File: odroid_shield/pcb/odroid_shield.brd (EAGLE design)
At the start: 83 x 48 mm, 68 parts, among them J1 AVRISP6_COMPACT, J4 ODROID_J4, U1 SINGLE-BIT_BUS_TRANSCEIVER, U10 ABM8G, U2 SINGLE-BIT_BUS_TRANSCEIVER, U3 ST1S10, U4 ATMEGA644P-20AU, U5 TS5205, U6 TCA9517MSOP8, U7 MP33926, U8 MAX21000, U9 MMA8451Q

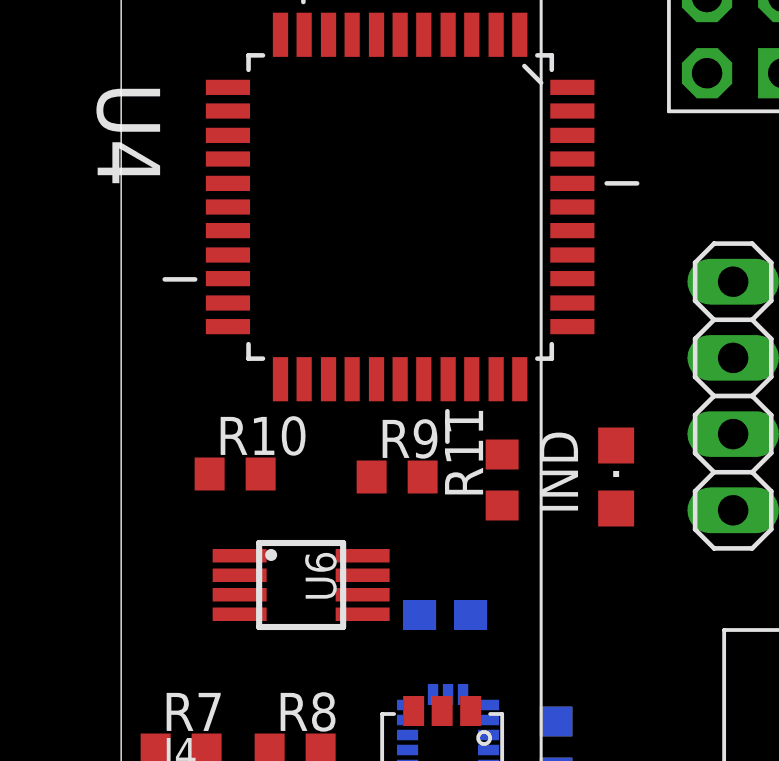
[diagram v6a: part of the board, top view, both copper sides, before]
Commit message: odroid_shield: Run schematic ERC.
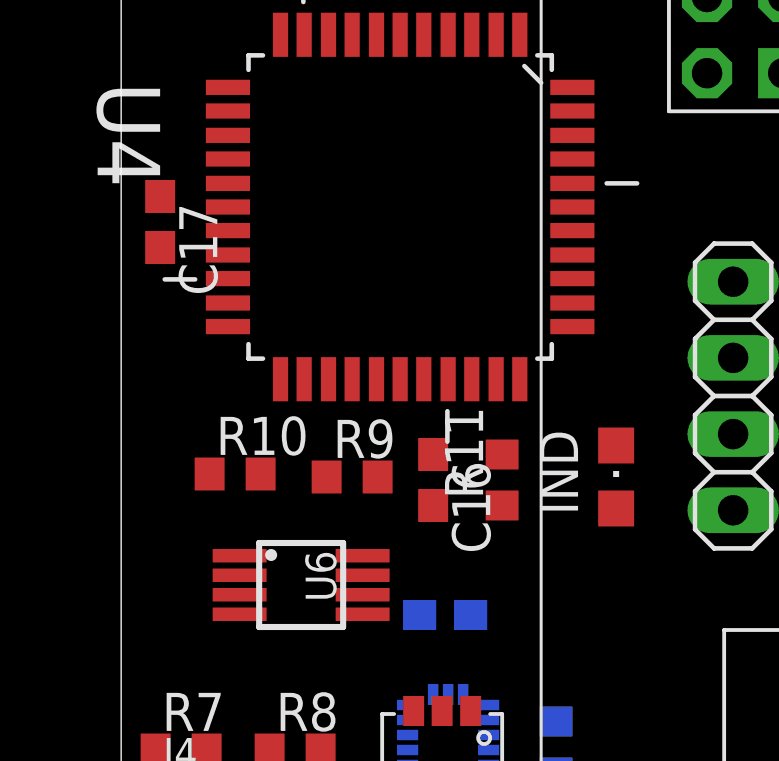
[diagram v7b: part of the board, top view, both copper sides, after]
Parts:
- added C16, C17: .1uF, rcl:C0603
- ARM: value (none) -> FLASH_RED
- D1, D2: value (none) -> 30V 2A
- IND: value (none) -> RED
- PWR: value (none) -> GREEN
- moved R9 1.50 mm to (7.70, 25.1)
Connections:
- new net N$30: C16.1, U4.29
- net +5V: now also C17.1
- net GND: now also C16.2, C17.2
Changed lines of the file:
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@@
 <element name="B+" library="odroid_shield" package="BAT_TERM" value="BAT_TERM" x="79.3" y="22.2" rot="MR0"/>
 <element name="B-" library="odroid_shield" package="BAT_TERM" value="BAT_TERM" x="73.5" y="22.2" rot="MR0"/>
-<element name="ARM" library="led" package="LED5MM" value="" x="29.8" y="28.6">
+<element name="ARM" library="led" package="LED5MM" value="FLASH_RED" x="29.8" y="28.6">
 <attribute name="DPN" value="67-1499-ND" x="29.8" y="28.6" size="1.778" layer="27" display="off"/>
 </element>
-<element name="PWR" library="led" package="CHIPLED_0805" value="" x="51.6" y="9.3" smashed="yes" rot="R270">
+<element name="PWR" library="led" package="CHIPLED_0805" value="GREEN" x="51.6" y="9.3" smashed="yes" rot="R270">
 <attribute name="NAME" x="53.93" y="8.67" size="1.27" layer="25"/>
 <attribute name="VALUE" x="50.33" y="6.76" size="1.27" layer="27"/>
@@
 <attribute name="NAME" x="44.265" y="8.835" size="1.27" layer="25"/>
 </element>
-<element name="D1" library="odroid_shield" package="CMS06" value="" x="44.7" y="3.2" rot="R180">
+<element name="D1" library="odroid_shield" package="CMS06" value="30V 2A" x="44.7" y="3.2" rot="R180">
 <attribute name="DPN" value="CMS06QMCT-ND" x="44.7" y="3.2" size="1.778" layer="27" rot="R180" display="off"/>
 </element>
-<element name="D2" library="odroid_shield" package="CMS06" value="" x="38" y="3.3">
+<element name="D2" library="odroid_shield" package="CMS06" value="30V 2A" x="38" y="3.3">
 <attribute name="DPN" value="CMS06QMCT-ND" x="38" y="3.3" size="1.778" layer="27" display="off"/>
 </element>
@@
 <attribute name="NAME" x="5.165" y="16.635" size="1.27" layer="25"/>
 </element>
-<element name="R9" library="rcl" package="R0603" value="4.7k" x="9.2" y="25.1" smashed="yes">
-<attribute name="NAME" x="8.565" y="25.735" size="1.27" layer="25"/>
+<element name="R9" library="rcl" package="R0603" value="4.7k" x="7.7" y="25.1" smashed="yes">
+<attribute name="NAME" x="7.065" y="25.735" size="1.27" layer="25"/>
 </element>
 <element name="R10" library="rcl" package="R0603" value="4.7k" x="3.8" y="25.2" smashed="yes">
@@
 </element>
 <element name="J1" library="odroid_shield" package="CON6P2R" value="AVRISP6_COMPACT" x="20.8" y="41.1" smashed="yes" rot="R90"/>
-<element name="IND" library="led" package="CHIPLED_0805" value="" x="16.5" y="25.1"/>
+<element name="IND" library="led" package="CHIPLED_0805" value="RED" x="16.5" y="25.1"/>
 <element name="SER2" library="pinhead" package="1X04" value="" x="20.4" y="27.8" rot="R270">
 <attribute name="DPN" value="S9410-ND" x="20.4" y="27.8" size="1" layer="27" ratio="10" rot="R270" display="off"/>
@@
 <element name="C15" library="rcl" package="C0603" value=".1uF" x="13.9" y="10.3" smashed="yes" rot="MR270">
 <attribute name="NAME" x="13.265" y="10.935" size="1.27" layer="26" rot="MR270"/>
+</element>
+<element name="C16" library="rcl" package="C0603" value=".1uF" x="10.4" y="25" smashed="yes" rot="R270">
+<attribute name="NAME" x="11.035" y="25.635" size="1.27" layer="25" rot="R270"/>
+</element>
+<element name="C17" library="rcl" package="C0603" value=".1uF" x="1.3" y="33.6" smashed="yes" rot="R270">
+<attribute name="NAME" x="1.935" y="34.235" size="1.27" layer="25" rot="R270"/>
 </element>
 </elements>
@@
 <contactref element="J1" pad="2"/>
 <contactref element="SER2" pad="4"/>
+<contactref element="C17" pad="1"/>
 <wire x1="45.8" y1="29" x2="43.55" y2="36.5" width="0" layer="19" extent="1-1"/>
 <wire x1="41.1" y1="21.45" x2="45.8" y2="29" width="0" layer="19" extent="1-1"/>
@@
 <wire x1="8.5126" y1="28.3596" x2="15.0404" y2="33.3126" width="0" layer="19" extent="1-1"/>
 <wire x1="3.5596" y1="34.1" x2="8.5126" y2="28.3596" width="0" layer="19" extent="1-1"/>
+<wire x1="1.3" y1="34.45" x2="3.5596" y2="34.1" width="0" layer="19" extent="1-1"/>
 </signal>
 <signal name="GND">
@@
 <contactref element="U3" pad="PAD5"/>
 <contactref element="U3" pad="PAD6"/>
+<contactref element="C16" pad="2"/>
+<contactref element="C17" pad="2"/>
 <wire x1="62.55" y1="38.9" x2="73.9" y2="37.25" width="0" layer="19" extent="16-16"/>
 <wire x1="57.284" y1="39.3398" x2="62.55" y2="38.9" width="0" layer="19" extent="16-16"/>
@@
 <wire x1="41.24" y1="12.195" x2="39.2" y2="13" width="0" layer="19" extent="1-1"/>
 <wire x1="35.96" y1="12.195" x2="38" y2="13" width="0" layer="19" extent="1-1"/>
-<wire x1="41.1" y1="7.5" x2="41.24" y2="12.195" width="0" layer="19" extent="1-1"/>
-<wire x1="44.65" y1="9.1" x2="41.1" y2="7.5" width="0" layer="19" extent="1-16"/>
+<wire x1="44.65" y1="9.1" x2="41.24" y2="12.195" width="0" layer="19" extent="1-16"/>
 <wire x1="45.35" y1="7.5" x2="44.65" y2="9.1" width="0" layer="19" extent="1-16"/>
+<wire x1="41.1" y1="7.5" x2="44.65" y2="9.1" width="0" layer="19" extent="1-16"/>
 <wire x1="52.65" y1="9.3" x2="45.35" y2="7.5" width="0" layer="19" extent="1-1"/>
 <wire x1="30.3" y1="5.75" x2="35.96" y2="12.195" width="0" layer="19" extent="1-16"/>
@@
 <wire x1="10.7" y1="17.3" x2="10.4" y2="15.15" width="0" layer="19" extent="1-16"/>
 <wire x1="9.95" y1="20.5" x2="10.7" y2="17.3" width="0" layer="19" extent="1-16"/>
+<wire x1="10.4" y1="24.15" x2="9.95" y2="20.5" width="0" layer="19" extent="1-16"/>
+<wire x1="9.3" y1="28.3596" x2="10.4" y2="24.15" width="0" layer="19" extent="1-1"/>
 <wire x1="3.95" y1="20.525" x2="9.95" y2="20.5" width="0" layer="19" extent="1-16"/>
-<wire x1="1.9" y1="7.5" x2="8.675" y2="9.8" width="0" layer="19" extent="16-16"/>
-<wire x1="9.3" y1="28.3596" x2="9.95" y2="20.5" width="0" layer="19" extent="1-16"/>
-<wire x1="16.5" y1="26.15" x2="9.3" y2="28.3596" width="0" layer="19" extent="1-1"/>
+<wire x1="16.5" y1="26.15" x2="10.4" y2="24.15" width="0" layer="19" extent="1-1"/>
 <wire x1="20.4" y1="31.61" x2="16.5" y2="26.15" width="0" layer="19" extent="1-1"/>
 <wire x1="15.0404" y1="34.1" x2="20.4" y2="31.61" width="0" layer="19" extent="1-1"/>
+<wire x1="1.9" y1="7.5" x2="8.675" y2="9.8" width="0" layer="19" extent="16-16"/>
 <wire x1="3.5596" y1="33.3126" x2="9.3" y2="28.3596" width="0" layer="19" extent="1-1"/>
 <wire x1="9.3" y1="39.8404" x2="15.0404" y2="34.1" width="0" layer="19" extent="1-1"/>
@@
 <wire x1="15.7" y1="42.65" x2="13.4" y2="42.85" width="0" layer="19" extent="1-1"/>
 <wire x1="19.53" y1="43.64" x2="15.7" y2="42.65" width="0" layer="19" extent="1-1"/>
+<wire x1="1.3" y1="32.75" x2="3.5596" y2="33.3126" width="0" layer="19" extent="1-1"/>
 <wire x1="57.6" y1="24.55" x2="47.4" y2="20.6" width="0" layer="19" extent="1-1"/>
 <wire x1="65.9" y1="24.55" x2="57.6" y2="24.55" width="0" layer="19" extent="1-1"/>
@@
 <wire x1="8.05" y1="20.525" x2="10.4" y2="17.85" width="0" layer="19" extent="1-16"/>
 <wire x1="8.05" y1="22.475" x2="8.05" y2="20.525" width="0" layer="19" extent="1-1"/>
-<wire x1="10.05" y1="25.1" x2="8.05" y2="22.475" width="0" layer="19" extent="1-1"/>
-<wire x1="4.65" y1="25.2" x2="8.05" y2="22.475" width="0" layer="19" extent="1-1"/>
+<wire x1="8.55" y1="25.1" x2="8.05" y2="22.475" width="0" layer="19" extent="1-1"/>
+<wire x1="4.65" y1="25.2" x2="8.55" y2="25.1" width="0" layer="19" extent="1-1"/>
 </signal>
 <signal name="N$19">
@@
 <contactref element="U8" pad="6"/>
 <contactref element="U9" pad="6"/>
-<wire x1="8.35" y1="25.1" x2="3.5596" y2="31.7124" width="0" layer="19" extent="1-1"/>
-<wire x1="8.05" y1="21.175" x2="8.35" y2="25.1" width="0" layer="19" extent="1-1"/>
+<wire x1="6.85" y1="25.1" x2="3.5596" y2="31.7124" width="0" layer="19" extent="1-1"/>
+<wire x1="8.05" y1="21.175" x2="6.85" y2="25.1" width="0" layer="19" extent="1-1"/>
 <wire x1="11.4" y1="15.15" x2="8.05" y2="21.175" width="0" layer="19" extent="1-16"/>
 <wire x1="10.5" y1="9.025" x2="11.4" y2="15.15" width="0" layer="19" extent="16-16"/>
@@
 <wire x1="6.9124" y1="28.3596" x2="57.284" y2="37.4094" width="0" layer="19" extent="1-16"/>
 </signal>
+<signal name="N$30">
+<contactref element="C16" pad="1"/>
+<contactref element="U4" pad="29"/>
+<wire x1="10.0874" y1="28.3596" x2="10.4" y2="25.85" width="0" layer="19" extent="1-1"/>
+</signal>
 </signals>

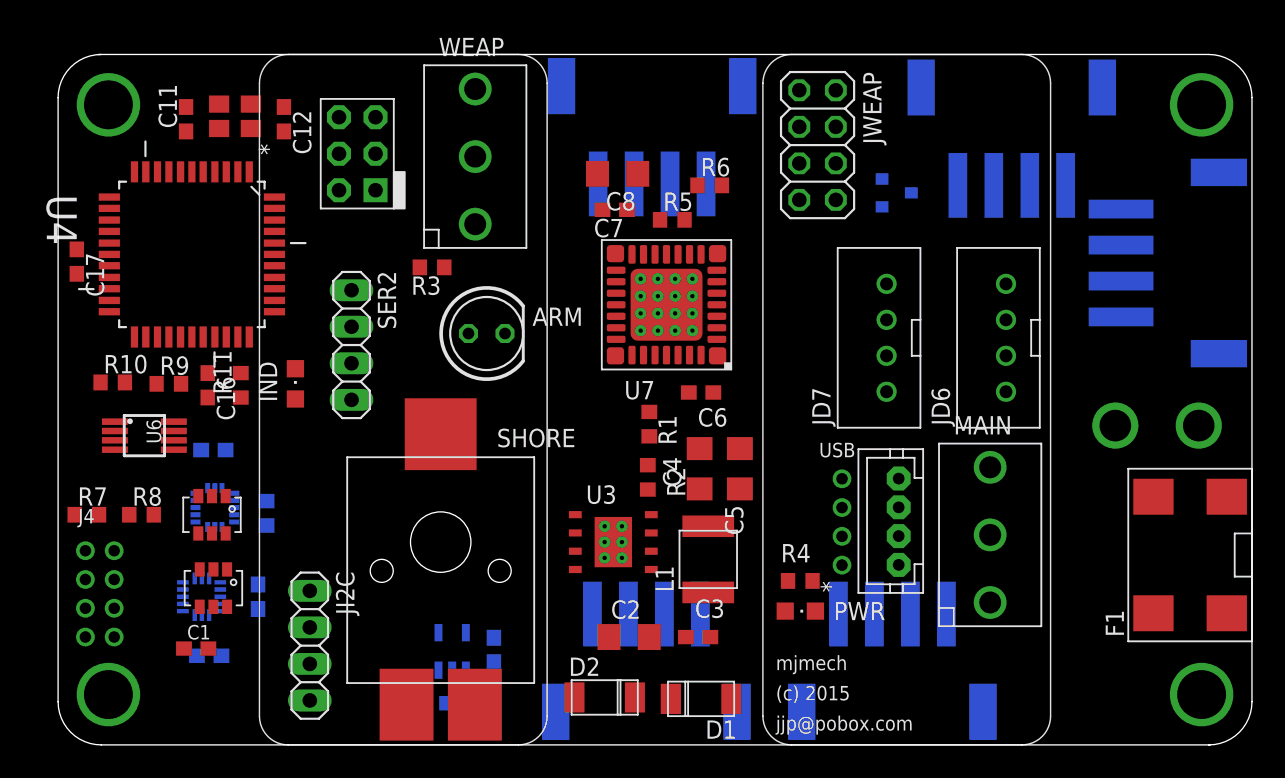
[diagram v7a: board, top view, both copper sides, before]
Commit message: odroid_shield: Working to line up and arrange parts using autorouter as a guide.
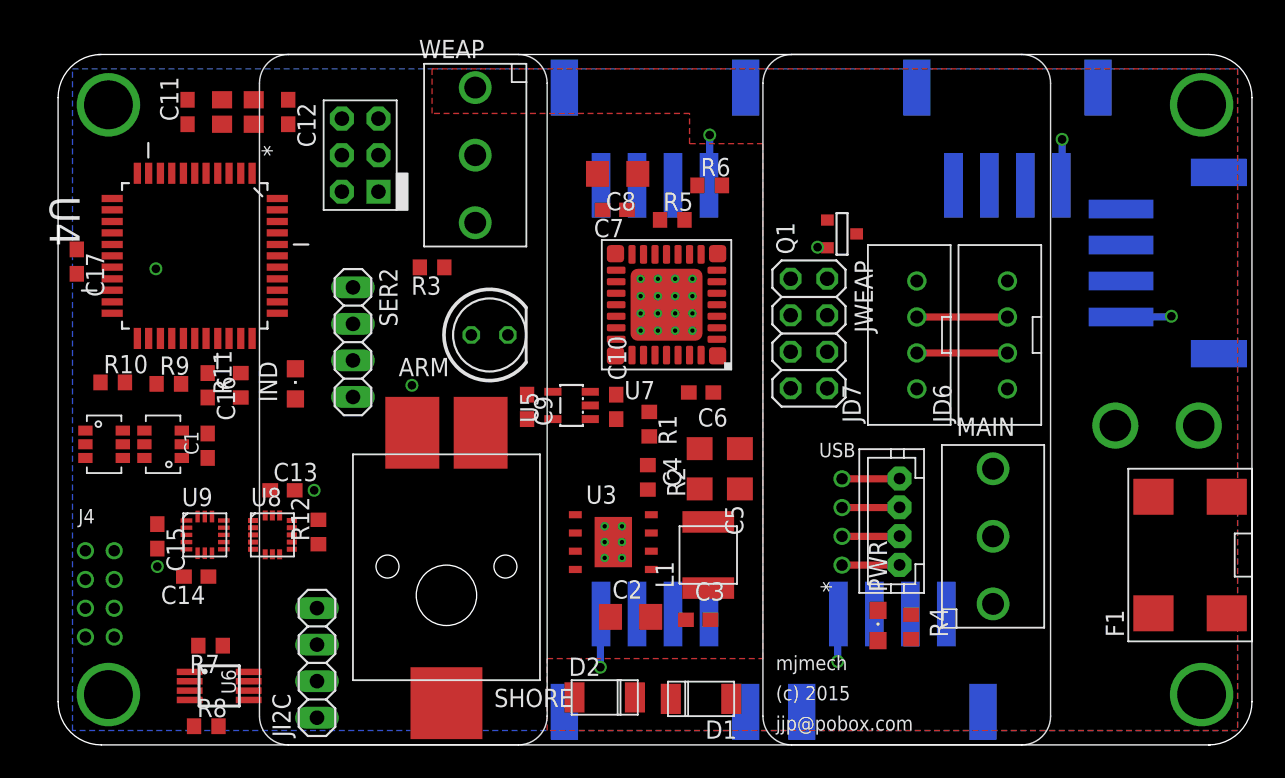
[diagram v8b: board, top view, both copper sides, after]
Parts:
- moved C10 23.3 mm to (38.8, 23.5), flipped to the top, turned to 270 degrees
- moved U5 19.0 mm to (35.7, 23.6), flipped to the top, turned to 90 degrees
- moved U6 18.2 mm to (11.2, 4.10)
- moved C9 17.1 mm to (32.6, 23.5), flipped to the top, turned to 90 degrees
- moved R8 15.4 mm to (10.3, 1.30)
- moved C1 14.1 mm to (10.4, 20.8), turned to 90 degrees
- moved JWEAP 13.1 mm to (52.2, 28.6)
- moved R7 12.5 mm to (10.6, 6.90), turned to 180 degrees
- moved U2 10.6 mm to (7.30, 20.9), turned to 180 degrees
- moved U1 8.96 mm to (3.20, 20.9), turned to 0 degrees
- moved R4 8.34 mm to (59.3, 8.20), turned to 90 degrees
- moved C15 8.16 mm to (6.90, 14.5), flipped to the top
- moved C14 5.57 mm to (9.60, 11.7), flipped to the top
- moved C13 5.56 mm to (15.6, 17.7), flipped to the top
- moved PWR 5.49 mm to (57.0, 8.30), turned to 0 degrees
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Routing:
- net +8V: track 0.00 -> 17.4 mm, vias 0 -> 5
- net ODROID_TX_5V: track 0.00 -> 6.30 mm
- net ODROID_RX_5V: track 0.00 -> 6.30 mm
- net N$3: track 0.00 -> 4.02 mm
- net N$1: track 0.00 -> 4.02 mm
- net N$6: track 0.00 -> 4.02 mm
- net N$5: track 0.00 -> 4.02 mm
- added copper zone on layer 1, net +8V
- added copper zone on layer 16, net GND
